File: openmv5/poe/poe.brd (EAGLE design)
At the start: 35.6 x 44.4 mm, 51 parts, among them IC1 AG9905LP, J1 GMJXHT-MM-S-88, T1 PT61018PEL, U1 OPENMV5-BOTTOM

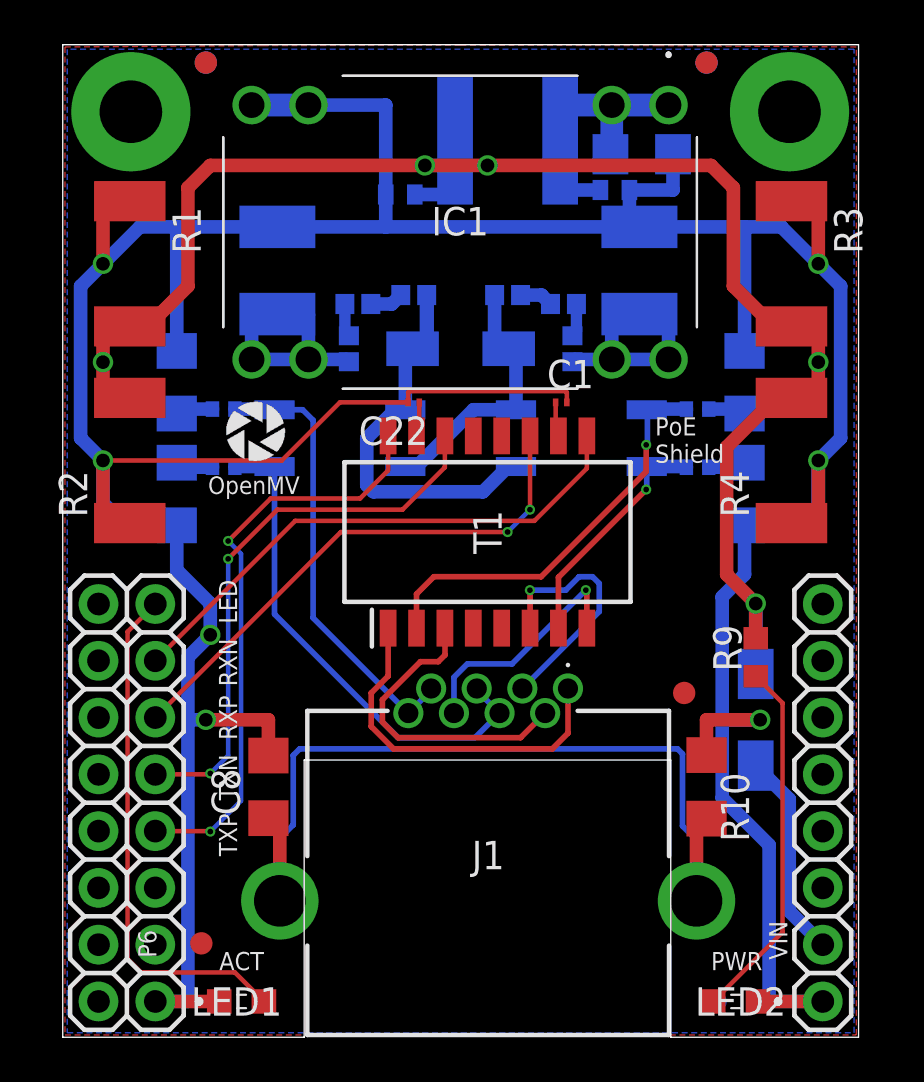
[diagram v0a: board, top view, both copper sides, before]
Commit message: Add labels to PoE shield
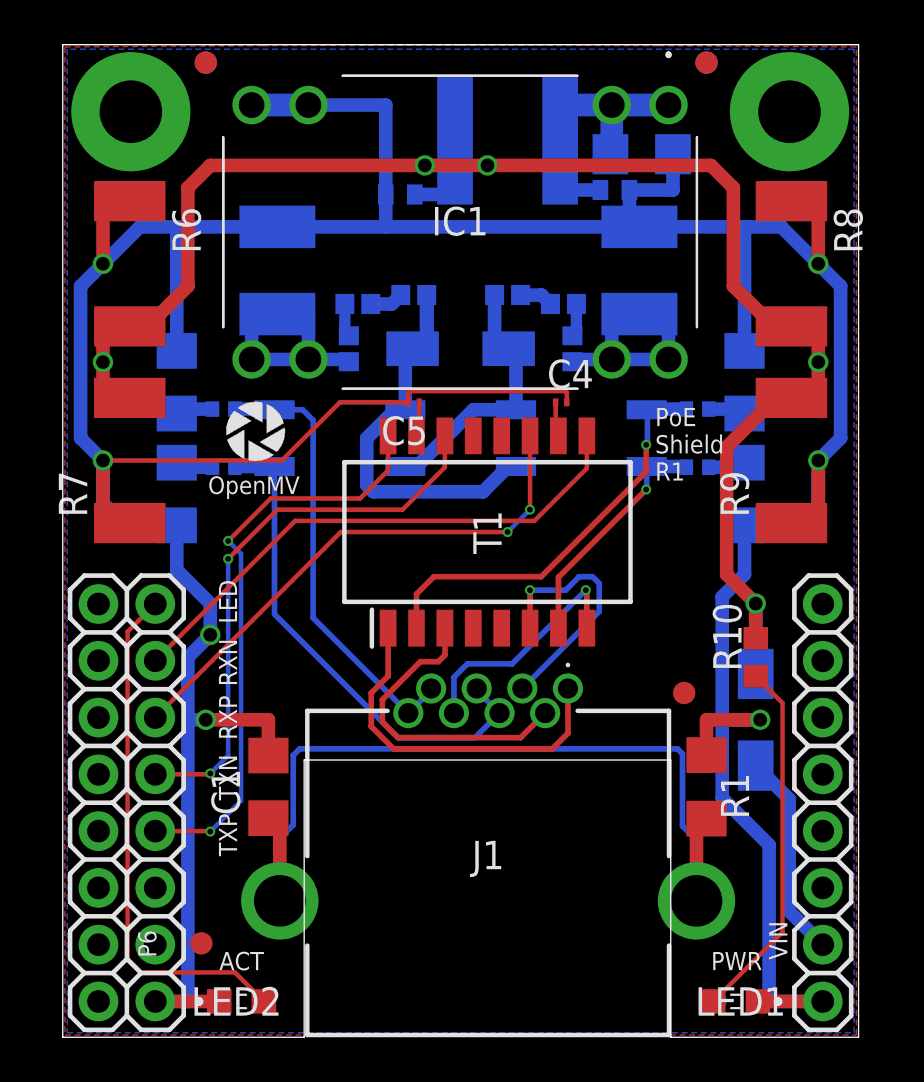
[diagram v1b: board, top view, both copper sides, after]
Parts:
- removed C22: 0.1uF, rcl:C0201
- added C12: 1nF, rcl:C1206
- C1: value 0.1uF -> 1nF; device rcl:C0201 -> rcl:C1206
- C10: value 4.7nF -> 1nF; device rcl:C1812 -> rcl:C1206
- C11: value 4.7nF -> 10uF; device rcl:C1812 -> rcl:C0402
- C2: value 100uF -> 4.7nF; device rcl:C1206 -> rcl:C1812
- C3: value 10uF -> 4.7nF; device rcl:C0402 -> rcl:C1812
- C4: value 10uF -> 0.1uF; device rcl:C0402 -> rcl:C0201
- C5: value 1nF -> 0.1uF; device rcl:C1206 -> rcl:C0201
- C6: value 1nF -> 100uF
- C7: value 1nF -> 10uF; device rcl:C1206 -> rcl:C0402
- D1: value FM240A -> SMAJ58A-13-F; device FM240A:DIOM5025X231N -> SMAJ58A-13-F:DIOM5226X230N
- D2: value SMAJ58A-13-F -> FM240A; device SMAJ58A-13-F:DIOM5226X230N -> FM240A:DIOM5025X231N
- L1: value NR6045T1R8N -> 1k; device NR6045T1R8N:NR6045T1R8N -> SparkFun-Coils:0402
- L7: value 1k -> NR6045T1R8N; device SparkFun-Coils:0402 -> NR6045T1R8N:NR6045T1R8N
- LED1: value LTST-S270KGKT -> LTST-S270KSKT
- LED2: value LTST-S270KSKT -> LTST-S270KGKT
- R1: value 100 -> 1M; device rcl:R2512 -> rcl:R1206
- R10: value 1M -> 470; device rcl:R1206 -> rcl:R0603
- R2, R3, R4: value 100 -> 75; device rcl:R2512 -> rcl:R0402
- R6, R7, R8: value 75 -> 100; device rcl:R0402 -> rcl:R2512
- R9: value 470 -> 100; device rcl:R0603 -> rcl:R2512
- moved FD4 47.8 mm to (29.2, 1.60), flipped to the bottom
- moved FD5 46.4 mm to (28.8, 43.6), flipped to the top
- moved FD6 42.0 mm to (28.8, 43.6)
- moved R1 34.8 mm to (28.8, 11.2)
- moved FD3 28.2 mm to (27.8, 15.4)
- moved C8 28.0 mm to (30.5, 29.3), flipped to the bottom
- moved R6 27.0 mm to (3.00, 34.6), flipped to the top, turned to 270 degrees
- moved R8 26.2 mm to (32.6, 34.6), flipped to the top, turned to 270 degrees
- moved R2 25.5 mm to (28.4, 28.1), flipped to the bottom, turned to 0 degrees
- moved R4 25.4 mm to (7.20, 25.5), flipped to the bottom, turned to 180 degrees
- moved C9 25.4 mm to (30.5, 24.3)
- moved FD2 23.3 mm to (9.00, 1.60), flipped to the bottom
- moved C10 23.0 mm to (5.10, 24.3), turned to 270 degrees
- moved FD7 22.4 mm to (6.40, 43.6), flipped to the top
- moved LED1 22.1 mm to (30.1, 1.60), turned to 180 degrees
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- renumbered U1 to J2
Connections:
- net GND: now also C12.2, R6.1, R7.1, R8.1, R9.1; no longer C22.2, R10.1, R2.1, R3.1, R4.1
- net MDI_LED: now also LED2.2; no longer LED1.2
- net MDI_RX_CT: now also C4.1; no longer C1.1
- net MDI_TX_CT: now also C5.1; no longer C22.1
- net POE_VIN_INT_N: now also C2.1; no longer C10.1
- net POE_VIN_INT_P: now also C3.1, L6.2; no longer C11.1, L2.2
- net POE_VIN_N: now also D1.2, L1.1; no longer D2.2, L7.1
- net POE_VIN_N0: now also L1.2, L3.1; no longer L6.1, L7.2
- net POE_VIN_N1: now also L3.2; no longer L6.2
- net POE_VIN_P: now also D1.1, L2.1; no longer D2.1, L4.1
- net POE_VIN_P0: now also L2.2, L4.1; no longer L3.1, L4.2
- net POE_VIN_P1: now also L4.2, L6.1; no longer L2.1, L3.2
- net SHIELD_GND: now also C1.1, R1.2; no longer C8.1, R10.2
- net VA1: now also R2.2; no longer R5.2
- net VA1_ISO: now also C8.1, R2.1; no longer C6.1, R5.1
- net VA2: now also R3.2; no longer R6.2
- net VA2_ISO: now also C9.1, R3.1; no longer C7.1, R6.1
- net VB1: now also R4.2; no longer R7.2
- net VB1_ISO: now also C10.1, R4.1; no longer C9.1, R7.1
- net VB2: now also R5.2; no longer R8.2
- net VB2_ISO: now also C12.1, R5.1; no longer C5.1, R8.1
- net VDC: now also C6.1, C7.1, L7.1; no longer C2.1, C3.1, L1.1
- net VIN: now also C11.1, D2.2, L7.2, R10.2, R6.2, R7.2, R8.2; no longer C4.1, D1.2, L1.2, R1.2, R2.2, R3.2, R4.2
- net VIN_INT: now also D2.1; no longer D1.1
- net VIN_LED: now also LED1.2, R10.1; no longer LED2.2, R9.1
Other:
- board text added: "Hot"
- board text added: "PoE Shield R1"
- board text removed: "PoE Shield"
